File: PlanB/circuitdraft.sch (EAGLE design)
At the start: 17 parts, among them Q1 16 MHz

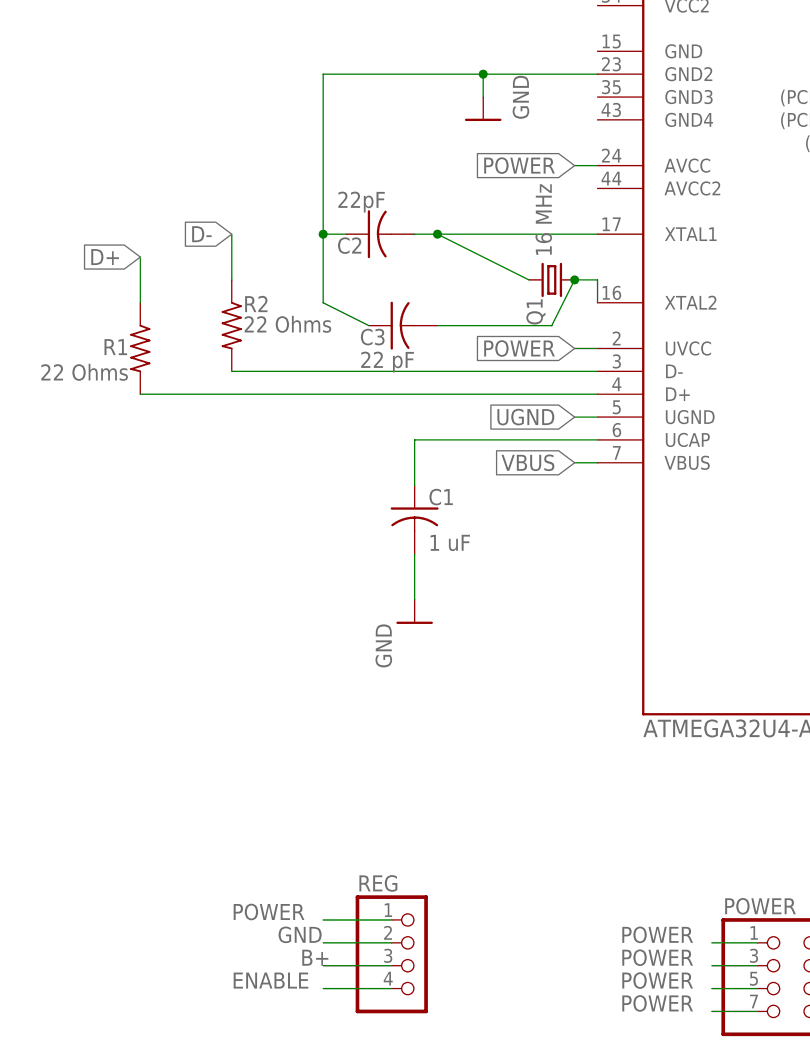
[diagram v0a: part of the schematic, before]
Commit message: using external board for charging, removes regulator, needs tweaking
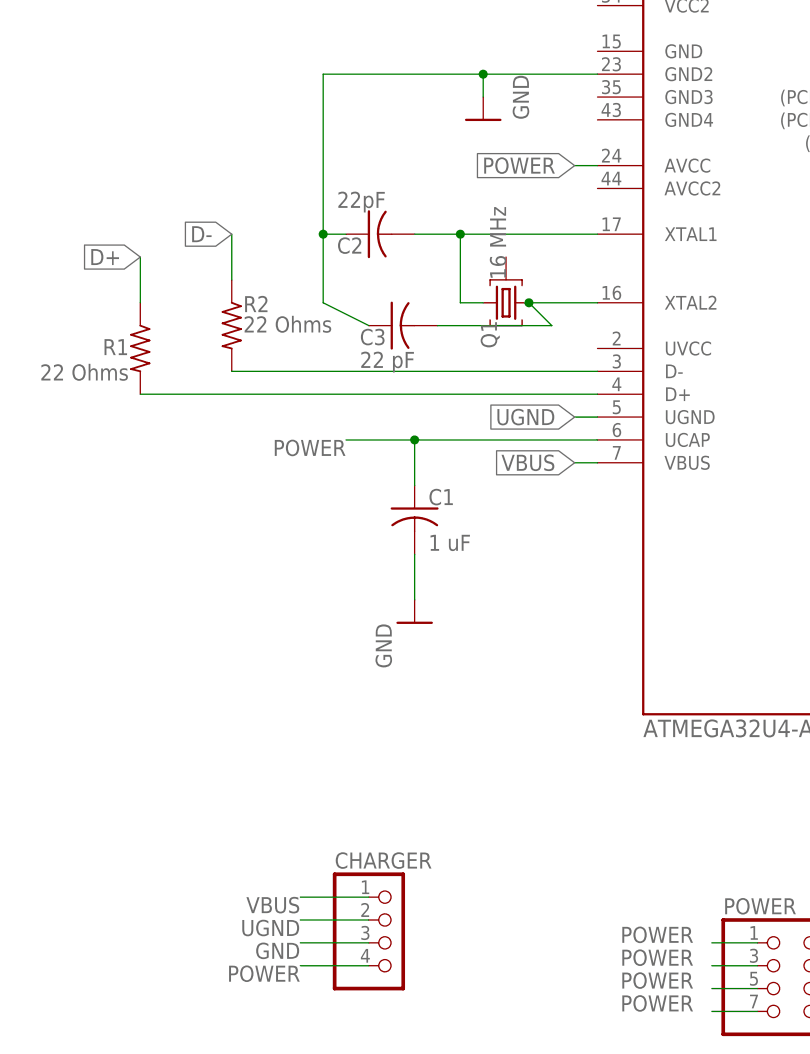
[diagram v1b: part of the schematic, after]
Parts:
- removed REG: (no value), pinhead:PINHD-1X4
- added CHARGER: (no value), pinhead:PINHD-1X4
- C2, C3: device rcl:C-USC0603 -> rcl:C-US025-024X044
- Q1: device crystal-geyer_V1_0:KX-5 -> crystal:10G7A-12.5KHZ
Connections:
- removed net B+: REG.3
- removed net ENABLE: REG.4
- removed net N$8: C1.1, U$1.UCAP
- net GND: now also CHARGER.3; no longer REG.2
- net N$6: now also Q1.3; no longer Q1.2
- net POWER: now also C1.1, CHARGER.4, U$1.UCAP; no longer REG.1, U$1.UVCC
- net UGND: now also CHARGER.2
- net VBUS: now also CHARGER.1

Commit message: added regulator
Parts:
- removed BU: (no value), pinhead:PINHD-1X1
- removed GROUND, POWER: (no value), pinhead:PINHD-2X4
- removed RBUTTON: 220 Ohm, rcl:R-US_R0603
- removed SERVO: (no value), pinhead:PINHD-1X5
- added BUTTON: (no value), pinhead:PINHD-1X2
- added REGIN, REGOUT, SERVO1, SERVO2, SERVO3, SERVO4, SERVO5: (no value), pinhead:PINHD-1X3
- LED, MYO: device pinhead:PINHD-1X1 -> pinhead:PINHD-1X3
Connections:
- removed net MIDDLE: U$1.(ADC7/TDI)PF7
- removed net MYOSIGNAL: MYO.1, U$1.(ADC0)PF0
- removed net UGND: CHARGER.2, U$1.UGND, USB.4
- new net N$1: MYO.3, U$1.(ADC0)PF0
- new net N$3: C1.1, U$1.UCAP
- new net VBAT: CHARGER.4, REGIN.1, U$1.(ADC7/TDI)PF7
- net GND: now also BUTTON.2, CHARGER.2, LED.3, MYO.2, REGIN.2, REGOUT.3, SERVO1.3, SERVO2.3, SERVO3.3, SERVO4.3, SERVO5.3, U$1.UGND, USB.4; no longer GROUND.1, GROUND.2, GROUND.3, GROUND.4, GROUND.5, GROUND.6, GROUND.7, GROUND.8, RBUTTON.2
- net INTERRUPT: now also BUTTON.1; no longer BU.1, RBUTTON.1
- net POWER: now also LED.2, MYO.1, REGOUT.2, SERVO1.2, SERVO2.2, SERVO3.2, SERVO4.2, SERVO5.2; no longer C1.1, CHARGER.4, POWER.1, POWER.2, POWER.3, POWER.4, POWER.5, POWER.6, POWER.7, POWER.8, U$1.UCAP
- net SIGNAL1: now also SERVO1.1; no longer SERVO.4
- net SIGNAL2: now also SERVO2.1; no longer SERVO.3
- net SIGNAL3: now also SERVO3.1; no longer SERVO.1
- net SIGNAL4: now also SERVO4.1; no longer SERVO.2
- net SIGNAL5: now also SERVO5.1; no longer SERVO.5

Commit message: ajusted to thorugh whole parts
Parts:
- C1: device rcl:C-USC0603 -> rcl:C-US025-024X044
- R1, R2: device rcl:R-US_R0603 -> rcl:R-US_0204/7
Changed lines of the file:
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@@
 <part name="U$1" library="mega32U4" deviceset="ATMEGA32U4-AU" device=""/>
 <part name="USB" library="pinhead" library_urn="urn:adsk.eagle:library:325" deviceset="PINHD-1X4" device="" package3d_urn="urn:adsk.eagle:package:22407/2"/>
-<part name="C1" library="rcl" library_urn="urn:adsk.eagle:library:334" deviceset="C-US" device="C0603" package3d_urn="urn:adsk.eagle:package:23616/2" value="1 uF"/>
+<part name="C1" library="rcl" library_urn="urn:adsk.eagle:library:334" deviceset="C-US" device="025-024X044" package3d_urn="urn:adsk.eagle:package:23630/1" value="1 uF"/>
 <part name="AGND1" library="supply1" library_urn="urn:adsk.eagle:library:371" deviceset="GND" device=""/>
-<part name="R1" library="rcl" library_urn="urn:adsk.eagle:library:334" deviceset="R-US_" device="R0603" package3d_urn="urn:adsk.eagle:package:23555/3" value="22 Ohms"/>
-<part name="R2" library="rcl" library_urn="urn:adsk.eagle:library:334" deviceset="R-US_" device="R0603" package3d_urn="urn:adsk.eagle:package:23555/3" value="22 Ohms"/>
+<part name="R1" library="rcl" library_urn="urn:adsk.eagle:library:334" deviceset="R-US_" device="0204/7" package3d_urn="urn:adsk.eagle:package:23498/2" value="22 Ohms"/>
+<part name="R2" library="rcl" library_urn="urn:adsk.eagle:library:334" deviceset="R-US_" device="0204/7" package3d_urn="urn:adsk.eagle:package:23498/2" value="22 Ohms"/>
 <part name="ISP" library="pinhead" library_urn="urn:adsk.eagle:library:325" deviceset="PINHD-2X3" device="" package3d_urn="urn:adsk.eagle:package:22462/2"/>
 <part name="AGND2" library="supply1" library_urn="urn:adsk.eagle:library:371" deviceset="GND" device=""/>
